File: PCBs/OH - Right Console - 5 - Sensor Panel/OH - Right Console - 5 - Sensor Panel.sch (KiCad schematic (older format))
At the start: 16 parts, among them J1 Input Coulmns, J2 Input Rows, SW1 FLIR_SW, SW2 LTD_R_SW, SW3 LST_NFLR_SW, SW4 LTD_R_ARM, SW5 RADAR_SW_PULL, SW6 SW_Rotary4, SW7 SW_Rotary8

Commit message: Panels
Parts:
- J1: footprint (none) -> PT_Library_v001:Molex_1x03_P2.54mm_Vertical
- J2, SW7: footprint (none) -> PT_Library_v001:Molex_1x08_P2.54mm_Vertical
- SW6: footprint (none) -> PT_Library_v001:Molex_1x04_P2.54mm_Vertical
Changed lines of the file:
@@
 F 0 "SW6" H 4850 4431 50  0000 C CNN
 F 1 "SW_Rotary4" H 4850 4340 50  0000 C CNN
-F 2 "" H 4750 4350 50  0001 C CNN
+F 2 "PT_Library_v001:Molex_1x04_P2.54mm_Vertical" H 4750 4350 50  0001 C CNN
 F 3 "" H 4750 4350 50  0001 C CNN
 	1    4950 3650
@@
 F 0 "SW7" H 4900 5781 50  0000 C CNN
 F 1 "SW_Rotary8" H 4900 5690 50  0000 C CNN
-F 2 "" H 4800 5700 50  0001 C CNN
+F 2 "PT_Library_v001:Molex_1x08_P2.54mm_Vertical" H 4800 5700 50  0001 C CNN
 F 3 "http://cdn-reichelt.de/documents/datenblatt/C200/DS-Serie%23LOR.pdf" H 4800 5700 50  0001 C CNN
 	1    5000 5000
@@
 F 0 "J2" H 6428 4676 50  0000 L CNN
 F 1 "Input Rows" H 6428 4585 50  0000 L CNN
-F 2 "" H 6400 4700 50  0001 C CNN
+F 2 "PT_Library_v001:Molex_1x08_P2.54mm_Vertical" H 6400 4700 50  0001 C CNN
 F 3 "~" H 6400 4700 50  0001 C CNN
 	1    6400 4700
@@
 F 0 "J1" H 992 3935 50  0000 C CNN
 F 1 "Input Coulmns" H 992 3844 50  0000 C CNN
-F 2 "" H 1100 3650 50  0001 C CNN
+F 2 "PT_Library_v001:Molex_1x03_P2.54mm_Vertical" H 1100 3650 50  0001 C CNN
 F 3 "~" H 1100 3650 50  0001 C CNN
 	1    1100 3650

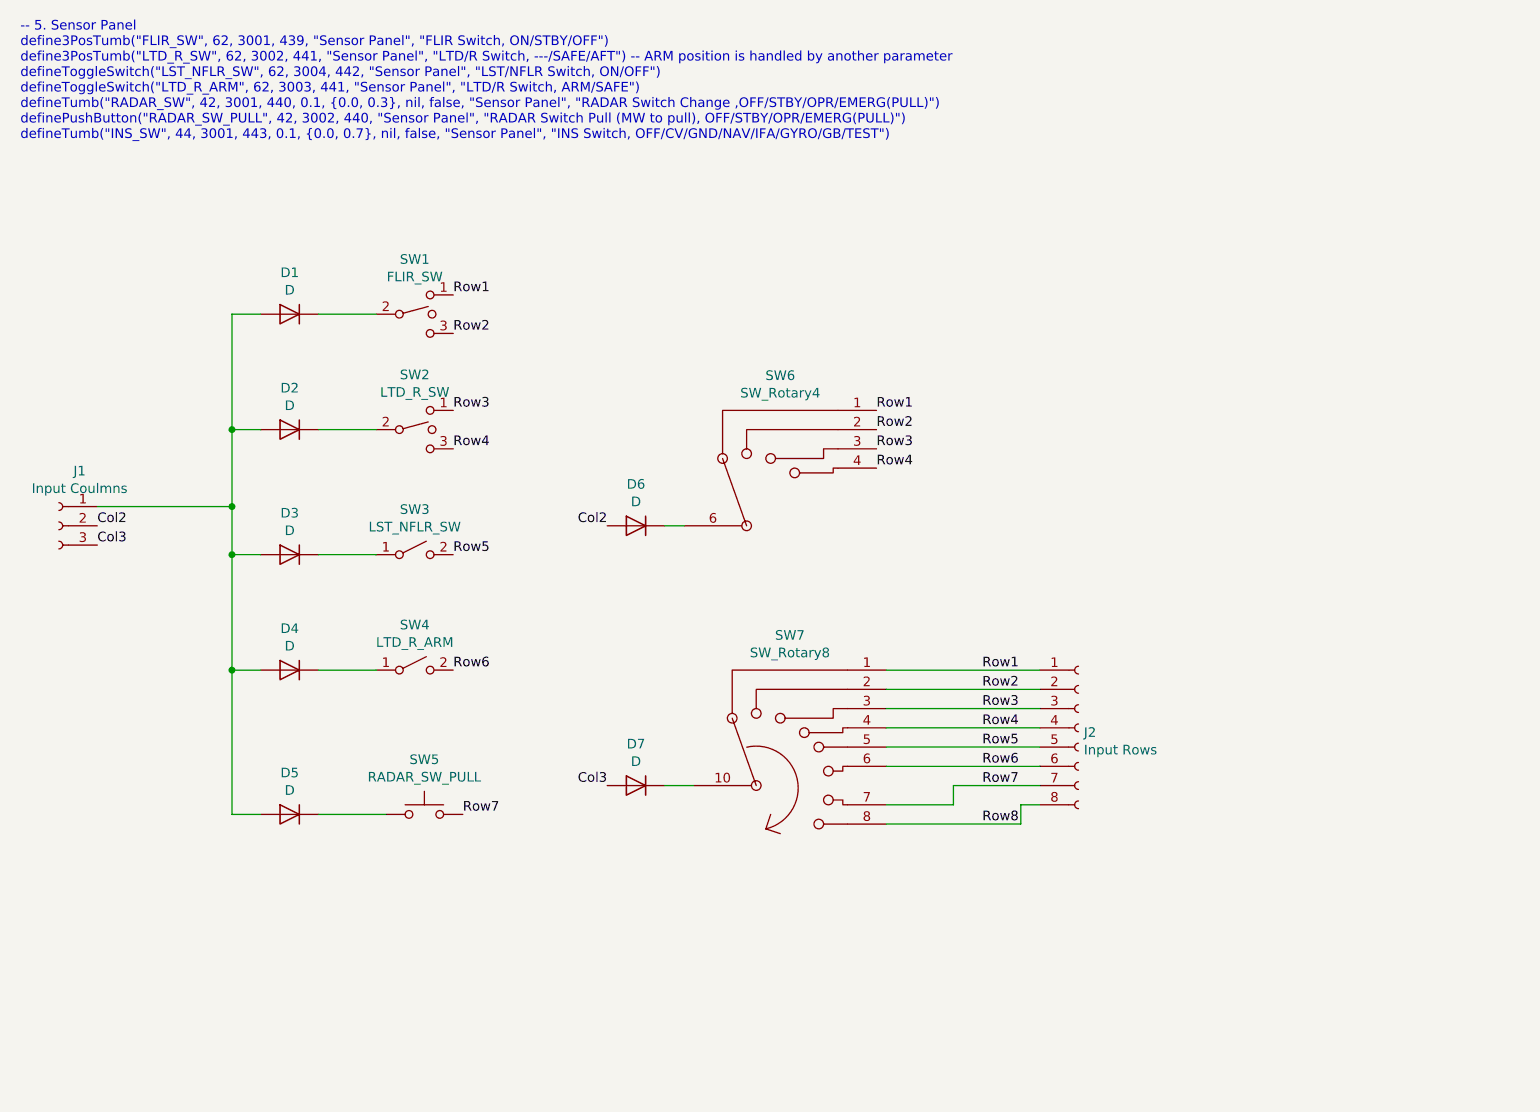
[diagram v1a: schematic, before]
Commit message: Sim Control Sensor
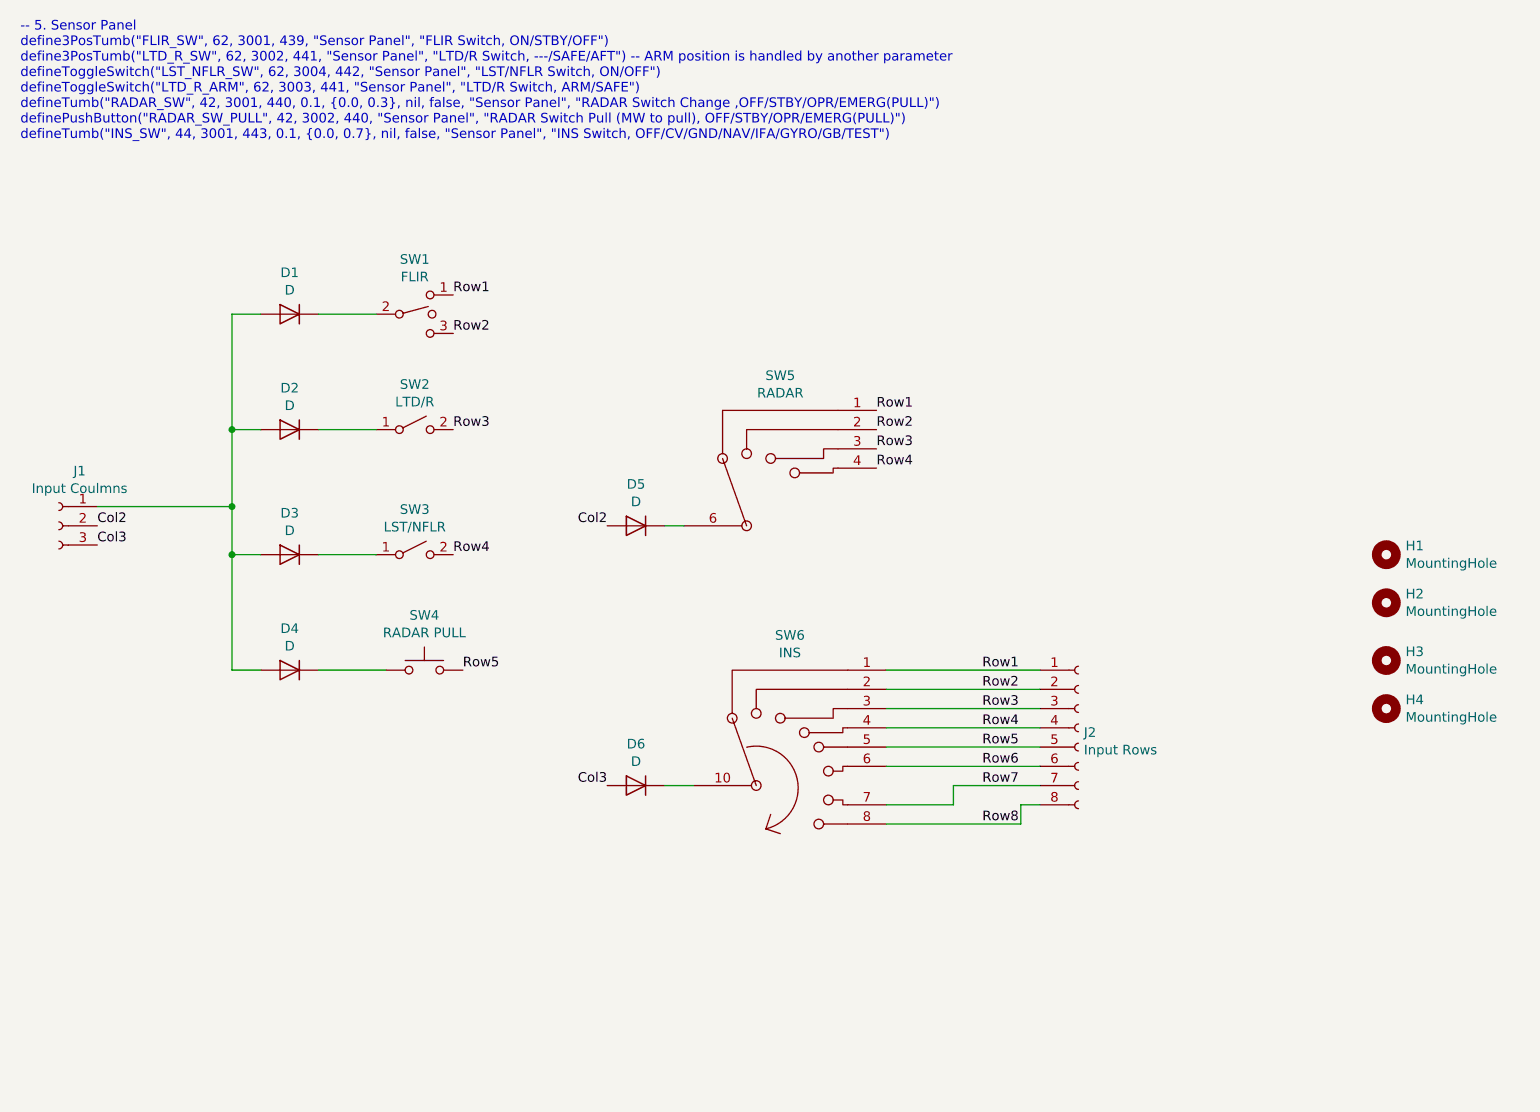
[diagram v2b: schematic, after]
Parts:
- removed D2: D, PT_Library_v001:D_Signal_P7.62mm_Horizontal, symbol Device:D
- removed SW2: LTD_R_SW, PT_Library_v001:Molex_1x03_P2.54mm_Vertical, symbol Switch:SW_SPDT_MSM
- removed SW6: SW_Rotary4, PT_Library_v001:Molex_1x04_P2.54mm_Vertical, symbol PT_Symbol_Library_v001:SW_Rotary4
- added H1, H2, H3, H4: MountingHole, MountingHole:MountingHole_3.2mm_M3, symbol Mechanical:MountingHole
- added SW5: RADAR, PT_Library_v001:Molex_1x06_P2.54mm_Vertical, symbol PT_Symbol_Library_v001:SW_Rotary4
- SW1: value FLIR_SW -> FLIR
- SW2: renamed from SW4; value LTD_R_ARM -> LTD/R
- SW3: value LST_NFLR_SW -> LST/NFLR
- SW4: renamed from SW5; value RADAR_SW_PULL -> RADAR PULL
- SW6: renamed from SW7; value SW_Rotary8 -> INS; footprint PT_Library_v001:Molex_1x08_P2.54mm_Vertical -> PT_Library_v001:Molex_1x10_P2.54mm_Vertical
- renumbered D4 to D2, D5 to D4, D6 to D5, D7 to D6
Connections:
- net Row1: now also SW5.1
- net Row2: now also SW5.2
- net Row3: now also SW2.2 (B), SW5.3
- net Row4: now also SW3.2 (B), SW5.4
- net Row5: now also SW4.2; no longer SW3.2 (B)
- net Row6: no longer SW2.2 (B)
- net Row7: no longer SW4.2
- net at D5.1 (K): now also SW5.6 (COM)
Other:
- moved on the sheet: D2, D4, SW2, SW4
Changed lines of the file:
@@
 P 2950 2550
 F 0 "SW1" H 2950 2835 50  0000 C CNN
-F 1 "FLIR_SW" H 2950 2744 50  0000 C CNN
+F 1 "FLIR" H 2950 2744 50  0000 C CNN
 F 2 "PT_Library_v001:Molex_1x03_P2.54mm_Vertical" H 2950 2550 50  0001 C CNN
 F 3 "~" H 2950 2550 50  0001 C CNN
@@
 $EndComp
 $Comp
-L Device:D D7
+L Device:D D6
 U 1 1 5FC2589C
 P 4100 5000
-F 0 "D7" H 4100 5216 50  0000 C CNN
+F 0 "D6" H 4100 5216 50  0000 C CNN
 F 1 "D" H 4100 5125 50  0000 C CNN
 F 2 "PT_Library_v001:D_Signal_P7.62mm_Horizontal" H 4100 5000 50  0001 C CNN
@@
 P 2950 3800
 F 0 "SW3" H 2950 4035 50  0000 C CNN
-F 1 "LST_NFLR_SW" H 2950 3944 50  0000 C CNN
+F 1 "LST/NFLR" H 2950 3944 50  0000 C CNN
 F 2 "PT_Library_v001:Molex_1x02_P2.54mm_Vertical" H 2950 3800 50  0001 C CNN
 F 3 "~" H 2950 3800 50  0001 C CNN
@@
 $EndComp
 $Comp
-L Switch:SW_Push SW5
+L Switch:SW_Push SW4
 U 1 1 5FC6A958
-P 3000 5150
-F 0 "SW5" H 3000 5435 50  0000 C CNN
-F 1 "RADAR_SW_PULL" H 3000 5344 50  0000 C CNN
-F 2 "PT_Library_v001:Molex_1x02_P2.54mm_Vertical" H 3000 5350 50  0001 C CNN
-F 3 "~" H 3000 5350 50  0001 C CNN
-	1    3000 5150
+P 3000 4400
+F 0 "SW4" H 3000 4685 50  0000 C CNN
+F 1 "RADAR PULL" H 3000 4594 50  0000 C CNN
+F 2 "PT_Library_v001:Molex_1x02_P2.54mm_Vertical" H 3000 4600 50  0001 C CNN
+F 3 "~" H 3000 4600 50  0001 C CNN
+	1    3000 4400
 	1    0    0    -1
 $EndComp
@@
 $EndBitmap
 $Comp
-L Switch:SW_SPDT_MSM SW2
-U 1 1 5FD2D380
+L Switch:SW_SPST SW2
+U 1 1 5FD2E318
 P 2950 3150
-F 0 "SW2" H 2950 3435 50  0000 C CNN
-F 1 "LTD_R_SW" H 2950 3344 50  0000 C CNN
-F 2 "PT_Library_v001:Molex_1x03_P2.54mm_Vertical" H 2950 3150 50  0001 C CNN
+F 0 "SW2" H 2950 3385 50  0000 C CNN
+F 1 "LTD/R" H 2950 3294 50  0000 C CNN
+F 2 "PT_Library_v001:Molex_1x02_P2.54mm_Vertical" H 2950 3150 50  0001 C CNN
 F 3 "~" H 2950 3150 50  0001 C CNN
 	1    2950 3150
@@
 $EndComp
 $Comp
-L Switch:SW_SPST SW4
-U 1 1 5FD2E318
-P 2950 4400
-F 0 "SW4" H 2950 4635 50  0000 C CNN
-F 1 "LTD_R_ARM" H 2950 4544 50  0000 C CNN
-F 2 "PT_Library_v001:Molex_1x02_P2.54mm_Vertical" H 2950 4400 50  0001 C CNN
-F 3 "~" H 2950 4400 50  0001 C CNN
-	1    2950 4400
-	1    0    0    -1
-$EndComp
-$Comp
-L PT_Symbol_Library_v001:SW_Rotary4 SW6
-U 1 1 5FD2F97E
-P 4950 3650
-F 0 "SW6" H 4850 4431 50  0000 C CNN
-F 1 "SW_Rotary4" H 4850 4340 50  0000 C CNN
-F 2 "PT_Library_v001:Molex_1x04_P2.54mm_Vertical" H 4750 4350 50  0001 C CNN
-F 3 "" H 4750 4350 50  0001 C CNN
-	1    4950 3650
-	1    0    0    -1
-$EndComp
-$Comp
-L PT_Symbol_Library_v001:SW_Rotary8 SW7
+L PT_Symbol_Library_v001:SW_Rotary8 SW6
 U 1 1 5FD325D9
 P 5000 5000
-F 0 "SW7" H 4900 5781 50  0000 C CNN
-F 1 "SW_Rotary8" H 4900 5690 50  0000 C CNN
-F 2 "PT_Library_v001:Molex_1x08_P2.54mm_Vertical" H 4800 5700 50  0001 C CNN
+F 0 "SW6" H 4900 5781 50  0000 C CNN
+F 1 "INS" H 4900 5690 50  0000 C CNN
+F 2 "PT_Library_v001:Molex_1x10_P2.54mm_Vertical" H 4800 5700 50  0001 C CNN
 F 3 "http://cdn-reichelt.de/documents/datenblatt/C200/DS-Serie%23LOR.pdf" H 4800 5700 50  0001 C CNN
 	1    5000 5000
@@
 $EndComp
 $Comp
-L Device:D D6
+L Device:D D5
 U 1 1 5FD3680E
 P 4100 3650
-F 0 "D6" H 4100 3866 50  0000 C CNN
+F 0 "D5" H 4100 3866 50  0000 C CNN
 F 1 "D" H 4100 3775 50  0000 C CNN
 F 2 "PT_Library_v001:D_Signal_P7.62mm_Horizontal" H 4100 3650 50  0001 C CNN
@@
 $EndComp
 $Comp
-L Device:D D2
-U 1 1 5FD3772E
-P 2300 3150
-F 0 "D2" H 2300 3366 50  0000 C CNN
-F 1 "D" H 2300 3275 50  0000 C CNN
-F 2 "PT_Library_v001:D_Signal_P7.62mm_Horizontal" H 2300 3150 50  0001 C CNN
-F 3 "~" H 2300 3150 50  0001 C CNN
-	1    2300 3150
-	-1   0    0    -1
-$EndComp
-$Comp
 L Device:D D3
 U 1 1 5FD37AD0
@@
 $EndComp
 $Comp
-L Device:D D4
+L Device:D D2
 U 1 1 5FD37F81
+P 2300 3150
+F 0 "D2" H 2300 3366 50  0000 C CNN
+F 1 "D" H 2300 3275 50  0000 C CNN
+F 2 "PT_Library_v001:D_Signal_P7.62mm_Horizontal" H 2300 3150 50  0001 C CNN
+F 3 "~" H 2300 3150 50  0001 C CNN
+	1    2300 3150
+	-1   0    0    -1
+$EndComp
+$Comp
+L Device:D D4
+U 1 1 5FD38861
 P 2300 4400
 F 0 "D4" H 2300 4616 50  0000 C CNN
@@
 	-1   0    0    -1
 $EndComp
-$Comp
-L Device:D D5
-U 1 1 5FD38861
-P 2300 5150
-F 0 "D5" H 2300 5366 50  0000 C CNN
-F 1 "D" H 2300 5275 50  0000 C CNN
-F 2 "PT_Library_v001:D_Signal_P7.62mm_Horizontal" H 2300 5150 50  0001 C CNN
-F 3 "~" H 2300 5150 50  0001 C CNN
-	1    2300 5150
-	-1   0    0    -1
-$EndComp
 Wire Wire Line
-	2800 5150 2450 5150
+	2800 4400 2450 4400
 Wire Wire Line
-	2750 4400 2450 4400
+	2750 3150 2450 3150
 Wire Wire Line
 	2750 3800 2450 3800
 Wire Wire Line
-	2750 3150 2450 3150
-Wire Wire Line
 	2750 2550 2450 2550
 Wire Wire Line
@@
 Text Label 3150 2650 0    50   ~ 0
 Row2
-Text Label 3150 3050 0    50   ~ 0
-Row3
-Text Label 3150 3250 0    50   ~ 0
-Row4
 Text Label 3150 3800 0    50   ~ 0
+Row4
+Text Label 3150 3150 0    50   ~ 0
+Row3
+Text Label 3200 4400 0    50   ~ 0
 Row5
-Text Label 3150 4400 0    50   ~ 0
-Row6
-Text Label 3200 5150 0    50   ~ 0
-Row7
 Text Label 5350 3050 0    50   ~ 0
 Row1
@@
 Col3
 Wire Wire Line
-	2000 2550 2000 3150
-Wire Wire Line
-	2000 5150 2150 5150
+	2000 4400 2150 4400
 Wire Wire Line
 	2000 2550 2150 2550
 Wire Wire Line
-	2150 4400 2000 4400
-Connection ~ 2000 4400
-Wire Wire Line
-	2000 4400 2000 5150
+	2150 3150 2000 3150
 Wire Wire Line
 	2150 3800 2000 3800
 Connection ~ 2000 3800
 Wire Wire Line
-	2000 3800 2000 4400
+	1300 3550 2000 3550
+Connection ~ 2000 3550
 Wire Wire Line
-	2150 3150 2000 3150
+	2000 3550 2000 3800
+$Comp
+L PT_Symbol_Library_v001:SW_Rotary4 SW5
+U 1 1 60681E61
+P 4950 3650
+F 0 "SW5" H 4850 4431 50  0000 C CNN
+F 1 "RADAR" H 4850 4340 50  0000 C CNN
+F 2 "PT_Library_v001:Molex_1x06_P2.54mm_Vertical" H 4750 4350 50  0001 C CNN
+F 3 "" H 4750 4350 50  0001 C CNN
+	1    4950 3650
+	1    0    0    -1
+$EndComp
+Wire Wire Line
+	2000 3800 2000 4400
 Connection ~ 2000 3150
 Wire Wire Line
 	2000 3150 2000 3550
 Wire Wire Line
-	1300 3550 2000 3550
-Connection ~ 2000 3550
-Wire Wire Line
-	2000 3550 2000 3800
+	2000 2550 2000 3150
+$Comp
+L Mechanical:MountingHole H1
+U 1 1 6068A7ED
+P 8000 3800
+F 0 "H1" H 8100 3846 50  0000 L CNN
+F 1 "MountingHole" H 8100 3755 50  0000 L CNN
+F 2 "MountingHole:MountingHole_3.2mm_M3" H 8000 3800 50  0001 C CNN
+F 3 "~" H 8000 3800 50  0001 C CNN
+	1    8000 3800
+	1    0    0    -1
+$EndComp
+$Comp
+L Mechanical:MountingHole H2
+U 1 1 6068AAFF
+P 8000 4050
+F 0 "H2" H 8100 4096 50  0000 L CNN
+F 1 "MountingHole" H 8100 4005 50  0000 L CNN
+F 2 "MountingHole:MountingHole_3.2mm_M3" H 8000 4050 50  0001 C CNN
+F 3 "~" H 8000 4050 50  0001 C CNN
+	1    8000 4050
+	1    0    0    -1
+$EndComp
+$Comp
+L Mechanical:MountingHole H3
+U 1 1 6068AE2B
+P 8000 4350
+F 0 "H3" H 8100 4396 50  0000 L CNN
+F 1 "MountingHole" H 8100 4305 50  0000 L CNN
+F 2 "MountingHole:MountingHole_3.2mm_M3" H 8000 4350 50  0001 C CNN
+F 3 "~" H 8000 4350 50  0001 C CNN
+	1    8000 4350
+	1    0    0    -1
+$EndComp
+$Comp
+L Mechanical:MountingHole H4
+U 1 1 6068B1A8
+P 8000 4600
+F 0 "H4" H 8100 4646 50  0000 L CNN
+F 1 "MountingHole" H 8100 4555 50  0000 L CNN
+F 2 "MountingHole:MountingHole_3.2mm_M3" H 8000 4600 50  0001 C CNN
+F 3 "~" H 8000 4600 50  0001 C CNN
+	1    8000 4600
+	1    0    0    -1
+$EndComp
 $EndSCHEMATC

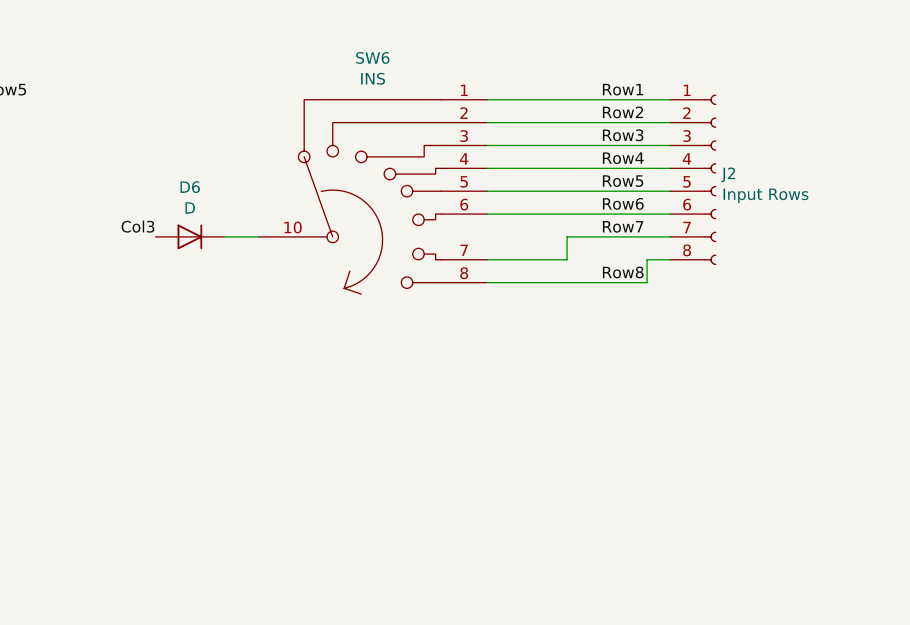
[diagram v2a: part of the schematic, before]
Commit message: Fix Sensor Panel Mag
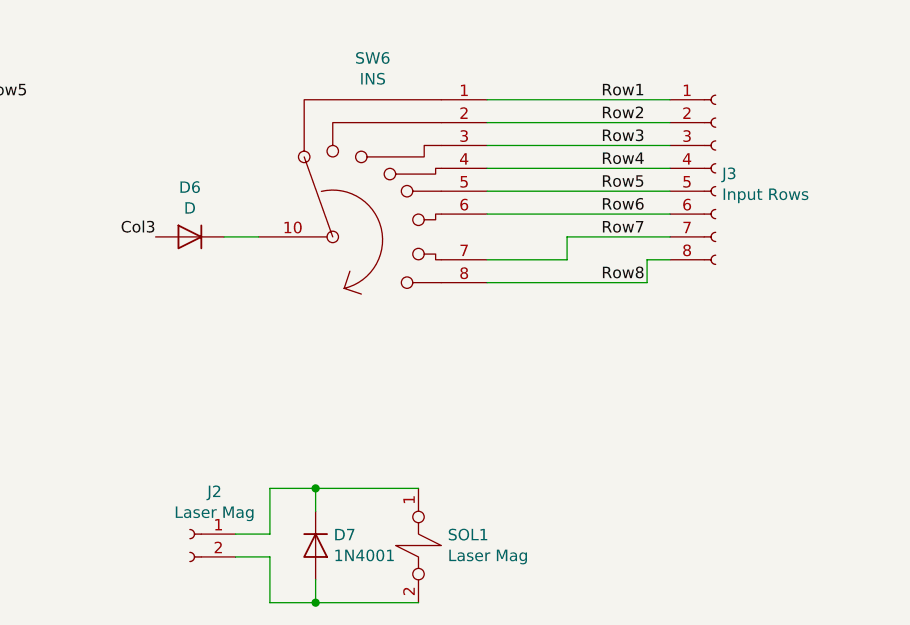
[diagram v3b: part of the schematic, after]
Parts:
- added D7: 1N4001, Diode_THT:D_DO-41_SOD81_P10.16mm_Horizontal, symbol Diode:1N4001
- added J2: Laser Mag, PT_Library_v001:Molex_1x02_P2.54mm_Vertical, symbol Connector:Conn_01x02_Female
- added SOL1: Laser Mag, PT_Library_v001:Molex_1x02_P2.54mm_Vertical, symbol OpenHornet:Solenoid
- renumbered J2 to J3
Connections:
- new net: D7.1 (K), J2.1 (Pin_1), SOL1.1
- new net: D7.2 (A), J2.2 (Pin_2), SOL1.2
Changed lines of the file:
@@
 $EndComp
 $Comp
-L Connector:Conn_01x08_Female J2
+L Connector:Conn_01x08_Female J3
 U 1 1 5FD352E6
 P 6400 4700
-F 0 "J2" H 6428 4676 50  0000 L CNN
+F 0 "J3" H 6428 4676 50  0000 L CNN
 F 1 "Input Rows" H 6428 4585 50  0000 L CNN
 F 2 "PT_Library_v001:Molex_1x08_P2.54mm_Vertical" H 6400 4700 50  0001 C CNN
@@
 	1    0    0    -1
 $EndComp
+$Comp
+L Connector:Conn_01x02_Female J2
+U 1 1 606A8C4C
+P 4100 6300
+F 0 "J2" H 3992 6485 50  0000 C CNN
+F 1 "Laser Mag" H 3992 6394 50  0000 C CNN
+F 2 "PT_Library_v001:Molex_1x02_P2.54mm_Vertical" H 4100 6300 50  0001 C CNN
+F 3 "~" H 4100 6300 50  0001 C CNN
+	1    4100 6300
+	-1   0    0    -1
+$EndComp
+$Comp
+L OpenHornet:Solenoid SOL1
+U 1 1 606AA8A0
+P 5100 6350
+F 0 "SOL1" V 5054 6478 50  0000 L CNN
+F 1 "Laser Mag" V 5145 6478 50  0000 L CNN
+F 2 "PT_Library_v001:Molex_1x02_P2.54mm_Vertical" H 5200 6250 197 0001 C CNN
+F 3 "" H 5200 6250 197 0001 C CNN
+	1    5100 6350
+	0    1    1    0
+$EndComp
+$Comp
+L Diode:1N4001 D7
+U 1 1 606AB890
+P 4650 6350
+F 0 "D7" V 4604 6429 50  0000 L CNN
+F 1 "1N4001" V 4695 6429 50  0000 L CNN
+F 2 "Diode_THT:D_DO-41_SOD81_P10.16mm_Horizontal" H 4650 6175 50  0001 C CNN
+F 3 "http://www.vishay.com/docs/88503/1n4001.pdf" H 4650 6350 50  0001 C CNN
+	1    4650 6350
+	0    1    1    0
+$EndComp
+Wire Wire Line
+	5100 6100 4650 6100
+Wire Wire Line
+	4450 6100 4450 6300
+Wire Wire Line
+	4450 6300 4300 6300
+Wire Wire Line
+	4300 6400 4450 6400
+Wire Wire Line
+	4450 6400 4450 6600
+Wire Wire Line
+	4450 6600 4650 6600
+Wire Wire Line
+	4650 6100 4650 6200
+Connection ~ 4650 6100
+Wire Wire Line
+	4650 6100 4450 6100
+Wire Wire Line
+	4650 6500 4650 6600
+Connection ~ 4650 6600
+Wire Wire Line
+	4650 6600 5100 6600
 $EndSCHEMATC

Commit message: RH PCBs
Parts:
- removed H2: MountingHole, MountingHole:MountingHole_3.2mm_M3, symbol Mechanical:MountingHole
- added H5, H6, H7: MountingHole, MountingHole:MountingHole_3.2mm_M3, symbol Mechanical:MountingHole
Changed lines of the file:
@@
-$EndComp
-$Comp
-L Mechanical:MountingHole H2
-U 1 1 6068AAFF
-P 8000 4050
-F 0 "H2" H 8100 4096 50  0000 L CNN
-F 1 "MountingHole" H 8100 4005 50  0000 L CNN
-F 2 "MountingHole:MountingHole_3.2mm_M3" H 8000 4050 50  0001 C CNN
-F 3 "~" H 8000 4050 50  0001 C CNN
-	1    8000 4050
-	1    0    0    -1
 $EndComp
 $Comp
@@
 Wire Wire Line
 	4650 6600 5100 6600
+$Comp
+L Mechanical:MountingHole H5
+U 1 1 6072A3FB
+P 8000 4850
+F 0 "H5" H 8100 4896 50  0000 L CNN
+F 1 "MountingHole" H 8100 4805 50  0000 L CNN
+F 2 "MountingHole:MountingHole_3.2mm_M3" H 8000 4850 50  0001 C CNN
+F 3 "~" H 8000 4850 50  0001 C CNN
+	1    8000 4850
+	1    0    0    -1
+$EndComp
+$Comp
+L Mechanical:MountingHole H6
+U 1 1 6072A94A
+P 8000 5100
+F 0 "H6" H 8100 5146 50  0000 L CNN
+F 1 "MountingHole" H 8100 5055 50  0000 L CNN
+F 2 "MountingHole:MountingHole_3.2mm_M3" H 8000 5100 50  0001 C CNN
+F 3 "~" H 8000 5100 50  0001 C CNN
+	1    8000 5100
+	1    0    0    -1
+$EndComp
+$Comp
+L Mechanical:MountingHole H7
+U 1 1 6072AEA6
+P 8000 5300
+F 0 "H7" H 8100 5346 50  0000 L CNN
+F 1 "MountingHole" H 8100 5255 50  0000 L CNN
+F 2 "MountingHole:MountingHole_3.2mm_M3" H 8000 5300 50  0001 C CNN
+F 3 "~" H 8000 5300 50  0001 C CNN
+	1    8000 5300
+	1    0    0    -1
+$EndComp
 $EndSCHEMATC
